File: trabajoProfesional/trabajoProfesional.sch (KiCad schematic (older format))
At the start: 21 parts, among them J1 SYSOUT, J2 BATPositve, J3 BATNegative, J4 GPIO5, J5 GPIO4, J6 GPIO3, J7 GPIO2, J8 GPIO1, U1 TS51224-M000WCSR

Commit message: se agregan todos los componentes al squematico
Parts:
- removed Cbst1, Cc1, Cc2, Cin1, Cout1, Cs1: C, Capacitor_SMD:C_1206_3216Metric, symbol Device:C
- removed J1: SYSOUT, Connector_Pin:Pin_D1.0mm_L10.0mm, symbol Connector_Generic:Conn_01x01
- removed J2: BATPositve, Connector_Pin:Pin_D1.0mm_L10.0mm, symbol Connector_Generic:Conn_01x01
- removed J3: BATNegative, Connector_Pin:Pin_D1.0mm_L10.0mm, symbol Connector_Generic:Conn_01x01
- removed J4: GPIO5, Connector_Pin:Pin_D1.0mm_L10.0mm, symbol Connector_Generic:Conn_01x01
- removed J5: GPIO4, Connector_Pin:Pin_D1.0mm_L10.0mm, symbol Connector_Generic:Conn_01x01
- removed J6: GPIO3, Connector_Pin:Pin_D1.0mm_L10.0mm, symbol Connector_Generic:Conn_01x01
- removed J7: GPIO2, Connector_Pin:Pin_D1.0mm_L10.0mm, symbol Connector_Generic:Conn_01x01
- removed J8: GPIO1, Connector_Pin:Pin_D1.0mm_L10.0mm, symbol Connector_Generic:Conn_01x01
- removed Lin1: L, Inductor_SMD:L_Neosid_Air-Coil_SML_6-10turn_HAM0631A-HAM1031A, symbol Device:L
- removed Lout1: L, Inductor_SMD:L_1206_3216Metric, symbol Device:L
- removed Rmod_cfg1, Rsense1, Rtherm1, Rtop1: R, Resistor_SMD:R_1206_3216Metric, symbol Device:R
- removed U1: TS51224-M000WCSR, TS51224-M000WCSR:BGA25N40P5X5_230X230X57N, symbol TS51224-M000WCSR:TS51224-M000WCSR
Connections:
- net labels removed: GND
- wire segments 52 -> 0

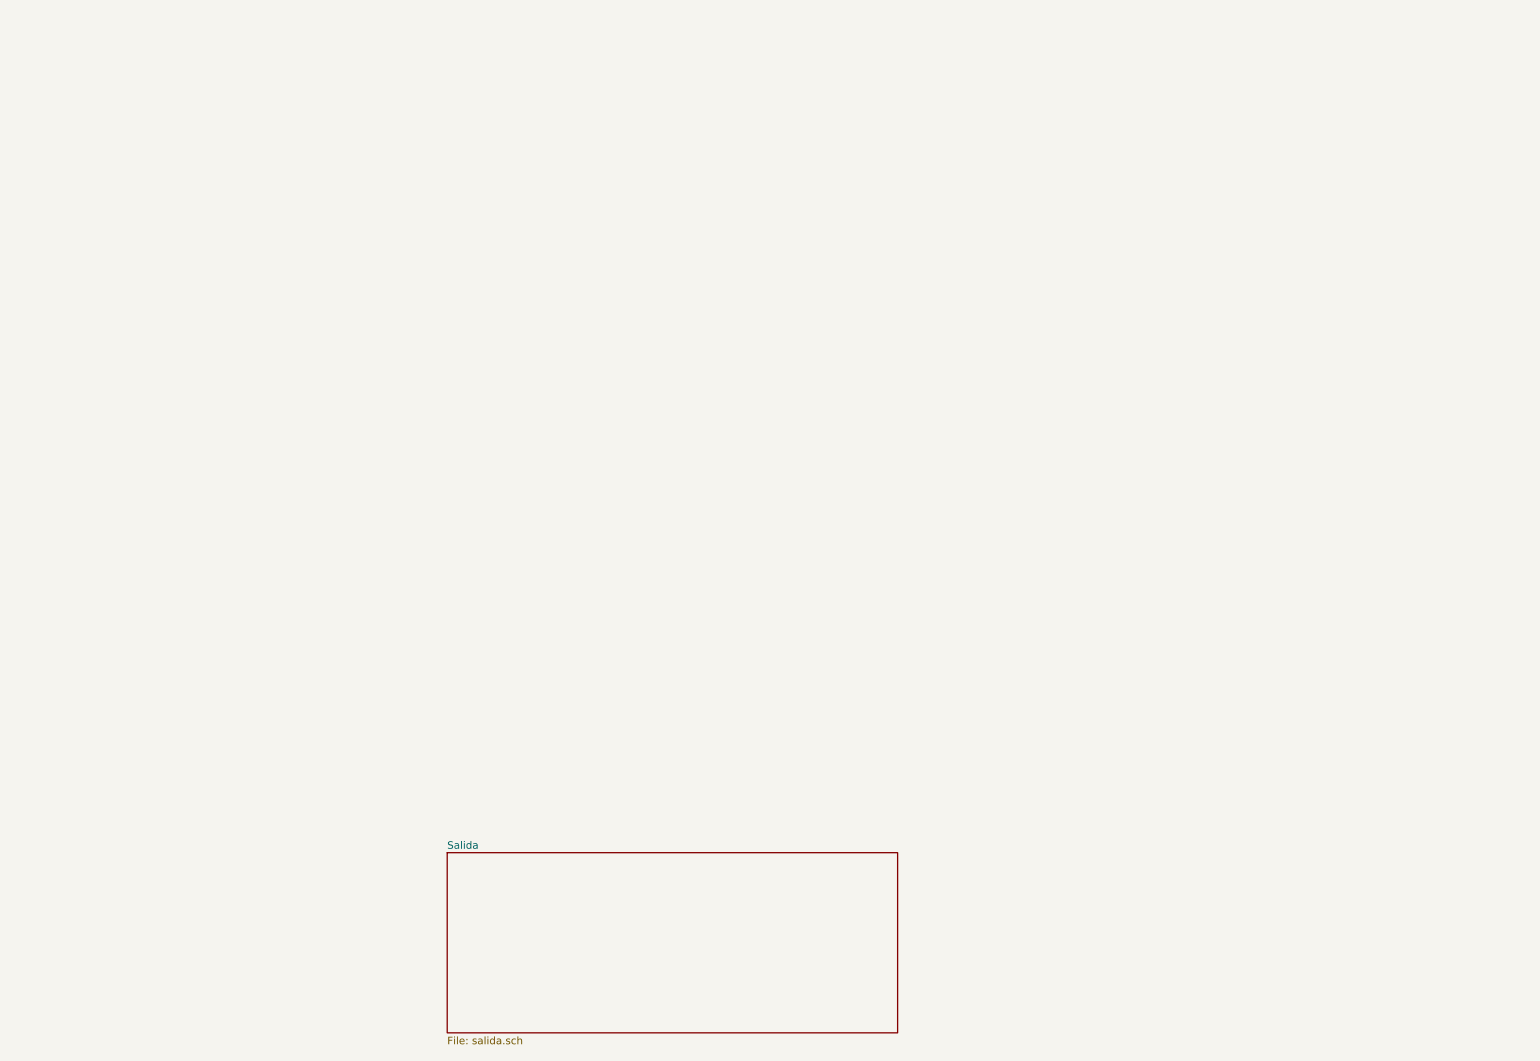
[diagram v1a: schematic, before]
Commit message: ya tenemos los modulos imlpementados en esquematicos, falta microprocesador
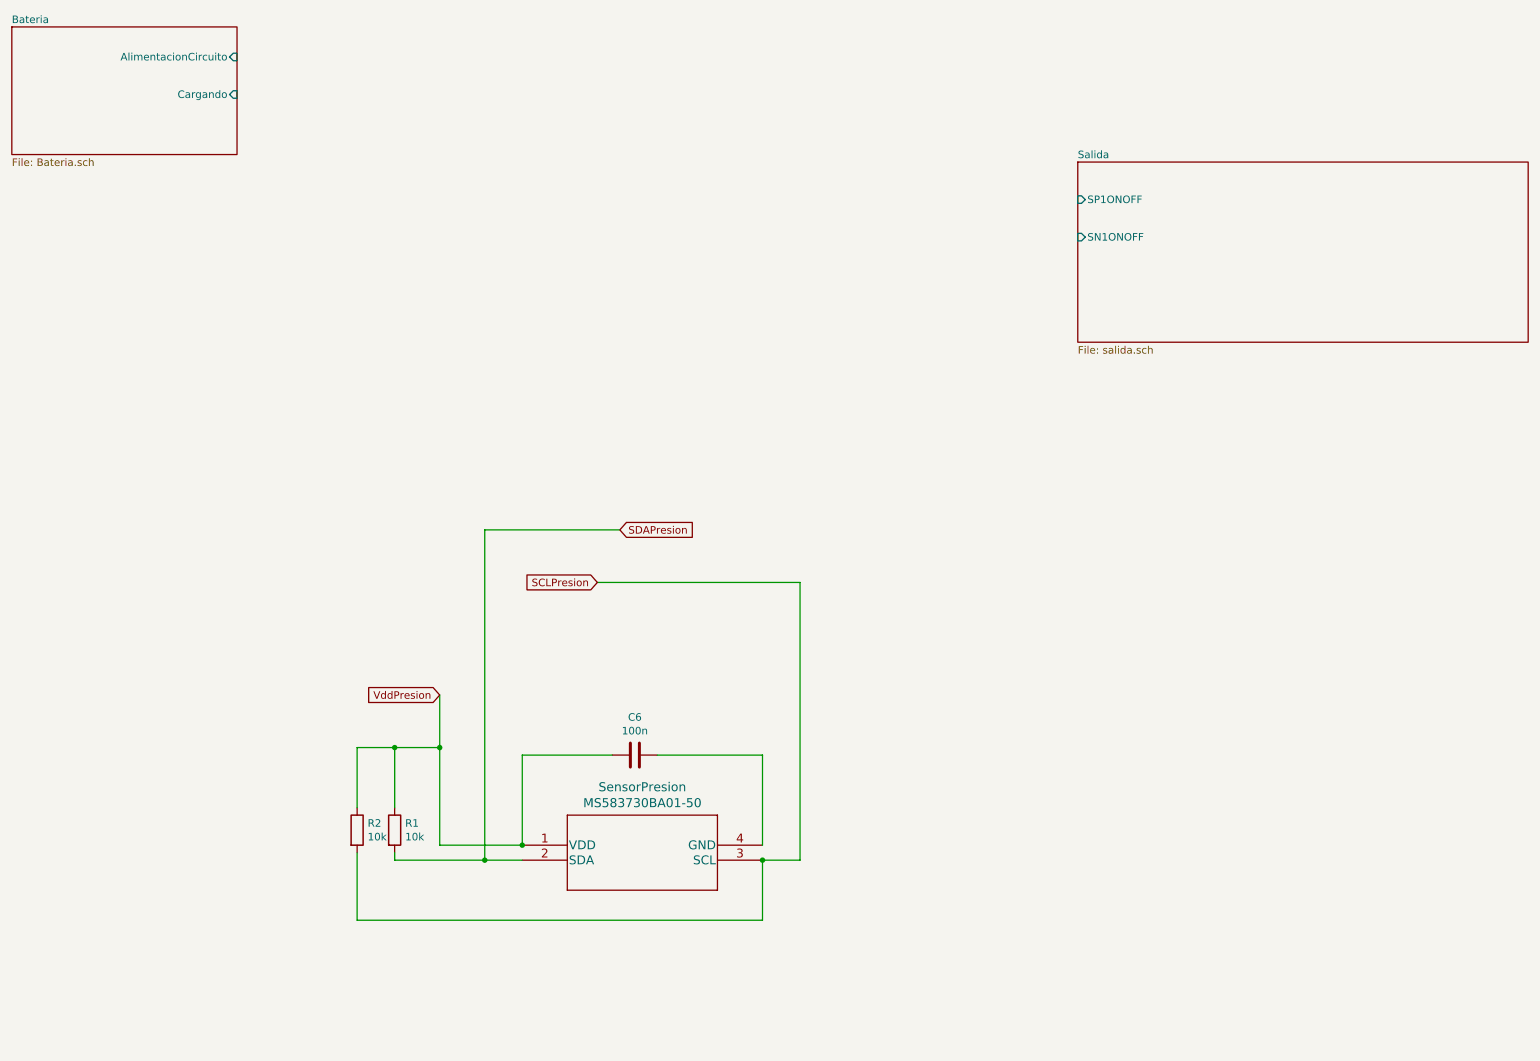
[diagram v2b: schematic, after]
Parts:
- added C6: 100n, symbol Device:C
- added R1, R2: 10k, symbol Device:R
- added SensorPresion: MS583730BA01-50, QFN4_MS5637_TEC, symbol 2020-08-16_19-32-11:MS583730BA01-50
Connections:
- new net: C6.1, SensorPresion.4 (GND)
- new net SCLPresion: R2.2, SensorPresion.3 (SCL)
- new net SDAPresion: R1.2, SensorPresion.2 (SDA)
- new net VddPresion: C6.2, R1.1, R2.1, SensorPresion.1 (VDD)
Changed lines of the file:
@@
 $Descr A4 11693 8268
 encoding utf-8
-Sheet 1 2
+Sheet 1 3
 Title ""
 Date ""
@@
 $EndDescr
 $Sheet
-S 3750 6350 3000 1200
+S 7950 1750 3000 1200
 U 5F3D0683
 F0 "Salida" 50
 F1 "salida.sch" 50
+F2 "SP1ONOFF" I L 7950 2000 50
+F3 "SN1ONOFF" I L 7950 2250 50
+$EndSheet
+$Comp
+L 2020-08-16_19-32-11:MS583730BA01-50 SensorPresion
+U 1 1 5F3E65FC
+P 4250 6300
+F 0 "SensorPresion" H 5050 6687 60  0000 C CNN
+F 1 "MS583730BA01-50" H 5050 6581 60  0000 C CNN
+F 2 "QFN4_MS5637_TEC" H 5050 6540 60  0001 C CNN
+F 3 "" H 4250 6300 60  0000 C CNN
+	1    4250 6300
+	1    0    0    -1
+$EndComp
+$Comp
+L Device:C C6
+U 1 1 5F3E7EA3
+P 5000 5700
+F 0 "C6" V 4748 5700 50  0000 C CNN
+F 1 "100n" V 4839 5700 50  0000 C CNN
+F 2 "" H 5038 5550 50  0001 C CNN
+F 3 "~" H 5000 5700 50  0001 C CNN
+	1    5000 5700
+	0    1    1    0
+$EndComp
+Wire Wire Line
+	5850 6300 5850 5700
+Wire Wire Line
+	5850 5700 5150 5700
+Wire Wire Line
+	4250 6300 4250 5700
+Wire Wire Line
+	4250 5700 4850 5700
+Text GLabel 3700 5300 0    50   Input ~ 0
+VddPresion
+Wire Wire Line
+	4250 6300 3700 6300
+Wire Wire Line
+	3700 6300 3700 5650
+Connection ~ 4250 6300
+$Comp
+L Device:R R1
+U 1 1 5F3E9874
+P 3400 6200
+F 0 "R1" H 3470 6246 50  0000 L CNN
+F 1 "10k" H 3470 6155 50  0000 L CNN
+F 2 "" V 3330 6200 50  0001 C CNN
+F 3 "~" H 3400 6200 50  0001 C CNN
+	1    3400 6200
+	1    0    0    -1
+$EndComp
+$Comp
+L Device:R R2
+U 1 1 5F3EA43A
+P 3150 6200
+F 0 "R2" H 3220 6246 50  0000 L CNN
+F 1 "10k" H 3220 6155 50  0000 L CNN
+F 2 "" V 3080 6200 50  0001 C CNN
+F 3 "~" H 3150 6200 50  0001 C CNN
+	1    3150 6200
+	1    0    0    -1
+$EndComp
+Wire Wire Line
+	3400 6050 3400 5650
+Wire Wire Line
+	3400 5650 3700 5650
+Connection ~ 3700 5650
+Wire Wire Line
+	3700 5650 3700 5300
+Wire Wire Line
+	3150 6050 3150 5650
+Wire Wire Line
+	3150 5650 3400 5650
+Connection ~ 3400 5650
+Wire Wire Line
+	3400 6350 3400 6400
+Wire Wire Line
+	3400 6400 4000 6400
+Wire Wire Line
+	5850 6400 5850 6800
+Wire Wire Line
+	5850 6800 3150 6800
+Wire Wire Line
+	3150 6800 3150 6350
+Text GLabel 4900 4200 2    50   Input ~ 0
+SDAPresion
+Text GLabel 4750 4550 0    50   Input ~ 0
+SCLPresion
+Wire Wire Line
+	4000 4200 4000 6400
+Connection ~ 4000 6400
+Wire Wire Line
+	4000 6400 4250 6400
+Wire Wire Line
+	5850 6400 6100 6400
+Wire Wire Line
+	6100 6400 6100 4550
+Wire Wire Line
+	6100 4550 4750 4550
+Connection ~ 5850 6400
+Wire Wire Line
+	4000 4200 4900 4200
+$Sheet
+S 850  850  1500 850
+U 5F3EBDF0
+F0 "Bateria" 50
+F1 "Bateria.sch" 50
+F2 "AlimentacionCircuito" I R 2350 1050 50
+F3 "Cargando" I R 2350 1300 50
 $EndSheet
 $EndSCHEMATC

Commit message: ya tenemos los componentes falta el micro
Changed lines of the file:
@@
 F2 "SP1ONOFF" I L 7950 2000 50
 F3 "SN1ONOFF" I L 7950 2250 50
+F4 "Alimentacion" I L 7950 2500 50
 $EndSheet
 $Comp

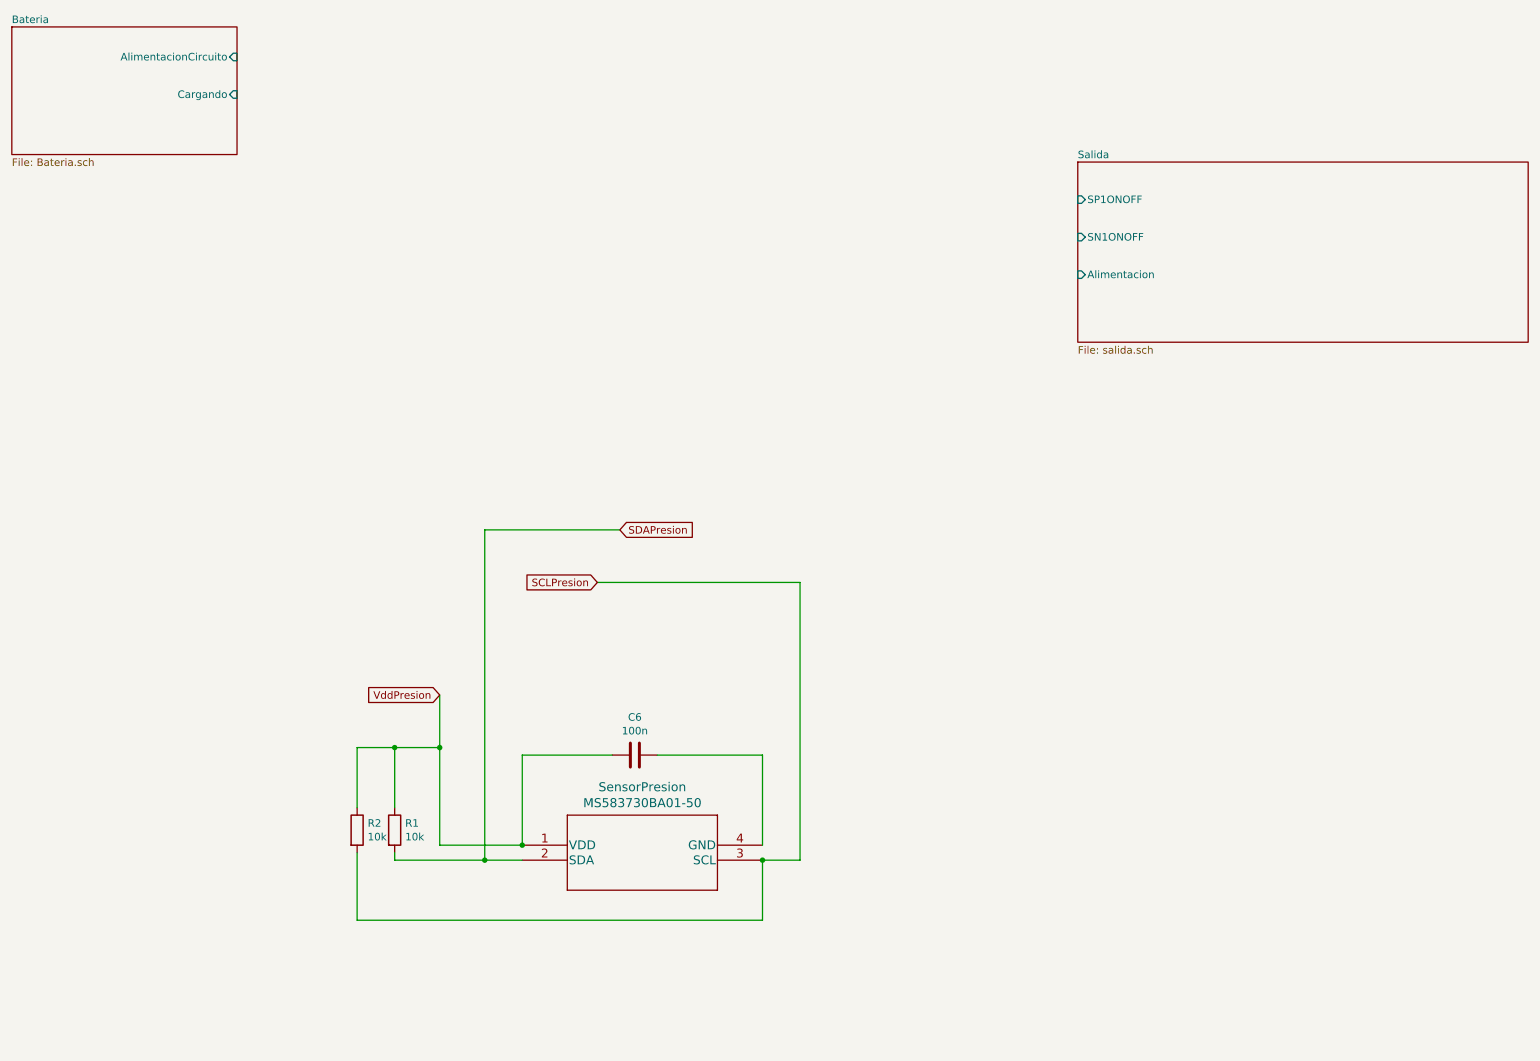
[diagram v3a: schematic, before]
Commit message: se agrego el Adafruit
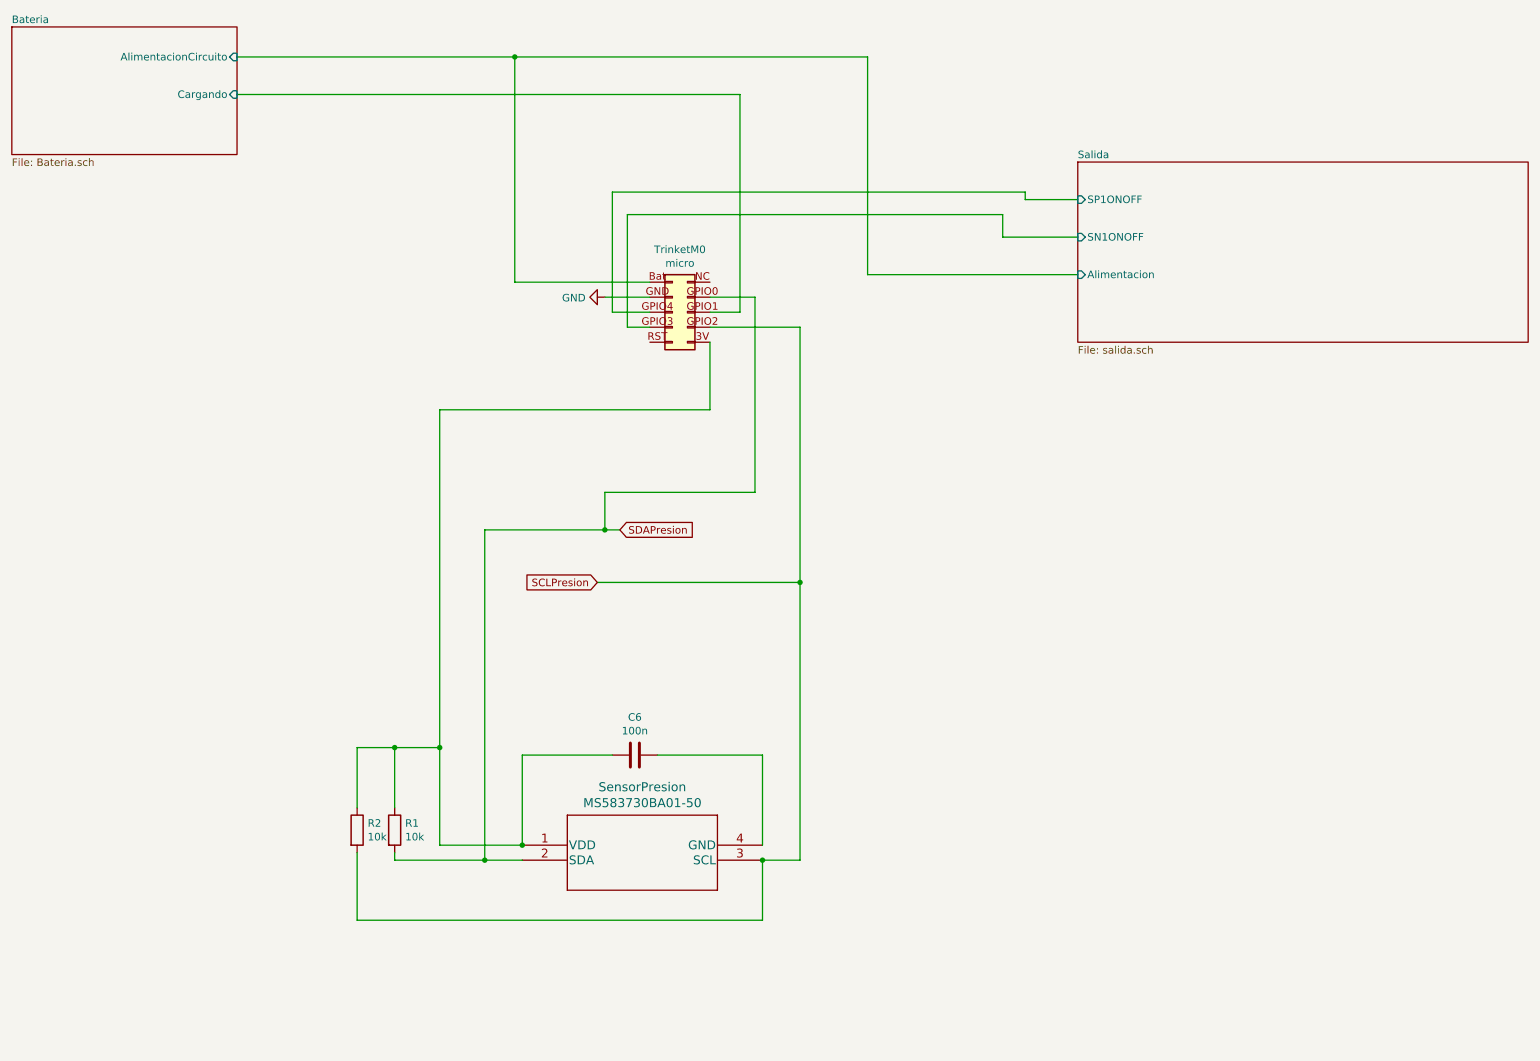
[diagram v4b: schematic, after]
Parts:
- added TrinketM0: micro, TrinketM0, symbol Connector_Generic:Conn_02x05_Row_Letter_First
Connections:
- net Bateria/AlimentacionCircuito: now also TrinketM0.Bat
- net Bateria/Cargando: now also TrinketM0.GPIO1
- net SCLPresion: now also TrinketM0.GPIO2
- net SDAPresion: now also TrinketM0.GPIO0
- net Salida/SN1ONOFF: now also TrinketM0.GPIO3
- net Salida/SP1ONOFF: now also TrinketM0.GPIO4
- net VddPresion: no longer names the net of C6.2, R1.1, R2.1, SensorPresion.1 (VDD)
- net VddPresion: now also TrinketM0.3V
- new net GND: TrinketM0.GND
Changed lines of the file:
@@
 Wire Wire Line
 	4250 5700 4850 5700
-Text GLabel 3700 5300 0    50   Input ~ 0
-VddPresion
 Wire Wire Line
 	4250 6300 3700 6300
@@
 Wire Wire Line
 	3400 5650 3700 5650
-Connection ~ 3700 5650
-Wire Wire Line
-	3700 5650 3700 5300
 Wire Wire Line
 	3150 6050 3150 5650
@@
 	6100 4550 4750 4550
 Connection ~ 5850 6400
-Wire Wire Line
-	4000 4200 4900 4200
 $Sheet
 S 850  850  1500 850
@@
 F3 "Cargando" I R 2350 1300 50
 $EndSheet
+$Comp
+L Connector_Generic:Conn_02x05_Row_Letter_First TrinketM0
+U 1 1 5F3DA13B
+P 5250 2750
+F 0 "TrinketM0" H 5300 3167 50  0000 C CNN
+F 1 "micro" H 5300 3076 50  0000 C CNN
+F 2 "TrinketM0" H 5250 2750 50  0001 C CNN
+F 3 "~" H 5250 2750 50  0001 C CNN
+	1    5250 2750
+	1    0    0    -1
+$EndComp
+Wire Wire Line
+	5100 2550 4200 2550
+Wire Wire Line
+	4200 2550 4200 1050
+Wire Wire Line
+	7950 2500 6550 2500
+Wire Wire Line
+	6550 2500 6550 1050
+Wire Wire Line
+	6550 1050 4200 1050
+Connection ~ 4200 1050
+$Comp
+L power:GND #PWR?
+U 1 1 5F3F217F
+P 4800 2650
+F 0 "#PWR?" H 4800 2400 50  0001 C CNN
+F 1 "GND" V 4805 2522 50  0000 R CNN
+F 2 "" H 4800 2650 50  0001 C CNN
+F 3 "" H 4800 2650 50  0001 C CNN
+	1    4800 2650
+	0    1    1    0
+$EndComp
+Wire Wire Line
+	5100 2650 4800 2650
+Wire Wire Line
+	2350 1050 4200 1050
+Wire Wire Line
+	5500 2950 5500 3400
+Wire Wire Line
+	5500 3400 3700 3400
+Wire Wire Line
+	3700 3400 3700 5650
+Connection ~ 3700 5650
+Wire Wire Line
+	6100 4550 6100 2850
+Wire Wire Line
+	6100 2850 5500 2850
+Connection ~ 6100 4550
+Wire Wire Line
+	4000 4200 4800 4200
+Wire Wire Line
+	4800 4200 4800 3950
+Wire Wire Line
+	4800 3950 5800 3950
+Wire Wire Line
+	5800 3950 5800 2650
+Wire Wire Line
+	5800 2650 5500 2650
+Connection ~ 4800 4200
+Wire Wire Line
+	4800 4200 4900 4200
+Wire Wire Line
+	5100 2750 4850 2750
+Wire Wire Line
+	4850 2750 4850 1950
+Wire Wire Line
+	4850 1950 7600 1950
+Wire Wire Line
+	7600 1950 7600 2000
+Wire Wire Line
+	7600 2000 7950 2000
+Wire Wire Line
+	5100 2850 4950 2850
+Wire Wire Line
+	4950 2850 4950 2100
+Wire Wire Line
+	4950 2100 7450 2100
+Wire Wire Line
+	7450 2100 7450 2250
+Wire Wire Line
+	7450 2250 7950 2250
+Wire Wire Line
+	5500 2750 5700 2750
+Wire Wire Line
+	5700 2750 5700 1300
+Wire Wire Line
+	5700 1300 2350 1300
 $EndSCHEMATC

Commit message: empezando el pcb
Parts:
- C6: footprint (none) -> Capacitor_SMD:C_2816_7142Metric
- R1, R2: footprint (none) -> Resistor_SMD:R_1206_3216Metric
- SensorPresion1: renamed from SensorPresion; footprint QFN4_MS5637_TEC -> Connector_PinSocket_2.54mm:PinSocket_2x02_P2.54mm_Vertical_SMD
- TrinketM0: footprint TrinketM0 -> Connector_PinHeader_1.00mm:PinHeader_2x05_P1.00mm_Vertical
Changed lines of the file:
@@
 $EndSheet
 $Comp
-L 2020-08-16_19-32-11:MS583730BA01-50 SensorPresion
+L 2020-08-16_19-32-11:MS583730BA01-50 SensorPresion1
 U 1 1 5F3E65FC
 P 4250 6300
-F 0 "SensorPresion" H 5050 6687 60  0000 C CNN
+F 0 "SensorPresion1" H 5050 6687 60  0000 C CNN
 F 1 "MS583730BA01-50" H 5050 6581 60  0000 C CNN
-F 2 "QFN4_MS5637_TEC" H 5050 6540 60  0001 C CNN
+F 2 "Connector_PinSocket_2.54mm:PinSocket_2x02_P2.54mm_Vertical_SMD" H 5050 6540 60  0001 C CNN
 F 3 "" H 4250 6300 60  0000 C CNN
 	1    4250 6300
@@
 F 0 "C6" V 4748 5700 50  0000 C CNN
 F 1 "100n" V 4839 5700 50  0000 C CNN
-F 2 "" H 5038 5550 50  0001 C CNN
+F 2 "Capacitor_SMD:C_2816_7142Metric" H 5038 5550 50  0001 C CNN
 F 3 "~" H 5000 5700 50  0001 C CNN
 	1    5000 5700
@@
 F 0 "R1" H 3470 6246 50  0000 L CNN
 F 1 "10k" H 3470 6155 50  0000 L CNN
-F 2 "" V 3330 6200 50  0001 C CNN
+F 2 "Resistor_SMD:R_1206_3216Metric" V 3330 6200 50  0001 C CNN
 F 3 "~" H 3400 6200 50  0001 C CNN
 	1    3400 6200
@@
 F 0 "R2" H 3220 6246 50  0000 L CNN
 F 1 "10k" H 3220 6155 50  0000 L CNN
-F 2 "" V 3080 6200 50  0001 C CNN
+F 2 "Resistor_SMD:R_1206_3216Metric" V 3080 6200 50  0001 C CNN
 F 3 "~" H 3150 6200 50  0001 C CNN
 	1    3150 6200
@@
 F 0 "TrinketM0" H 5300 3167 50  0000 C CNN
 F 1 "micro" H 5300 3076 50  0000 C CNN
-F 2 "TrinketM0" H 5250 2750 50  0001 C CNN
+F 2 "Connector_PinHeader_1.00mm:PinHeader_2x05_P1.00mm_Vertical" H 5250 2750 50  0001 C CNN
 F 3 "~" H 5250 2750 50  0001 C CNN
 	1    5250 2750
@@
 Connection ~ 4200 1050
 $Comp
-L power:GND #PWR?
+L power:GND #PWR0101
 U 1 1 5F3F217F
 P 4800 2650
-F 0 "#PWR?" H 4800 2400 50  0001 C CNN
+F 0 "#PWR0101" H 4800 2400 50  0001 C CNN
 F 1 "GND" V 4805 2522 50  0000 R CNN
 F 2 "" H 4800 2650 50  0001 C CNN
